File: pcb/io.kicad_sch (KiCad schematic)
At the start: 25 parts

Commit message: Further schematic capture
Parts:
- removed C? (x4): 100n, symbol Device:C
- removed J? (x2): PLR237, adatv2:PLx237, symbol adatv2:PLR237
- removed J? (x2): PLT237, adatv2:PLx237, symbol adatv2:PLT237
- removed L? (x2): 47u, symbol Device:L
- added D?: PRTR5V0U2X, Package_TO_SOT_SMD:SOT-143, symbol Power_Protection:PRTR5V0U2X
- added J?: WORD_CLK_4, symbol Connector:Conn_Coaxial
- added J?: WORD_CLK_3, symbol Connector:Conn_Coaxial
- added R? (x2): 75, symbol Device:R
- added U? (x4): 74LVC1G17, Package_TO_SOT_SMD:SOT-23-5, symbol 74xGxx:74LVC1G17
- R? (x2): value 1k -> 75
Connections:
- net +5V: now also D?.4 (VCC), U?.5 (VCC), U?.5 (VCC), U?.5 (VCC), U?.5 (VCC)
- net GND: now also D?.1 (GND), J?.2 (Ext), J?.2 (Ext), U?.3 (GND), U?.3 (GND), U?.3 (GND), U?.3 (GND)
- net WORD_CLK_1_75_OHM: no longer D?.3 (I/O2), J?.1 (In), R?.2
- net WORD_CLK_1: no longer names the net of R?.1
- net WORD_CLK_1: now also U?.4
- net WORD_CLK_2: no longer names the net of R?.1
- net WORD_CLK_2: now also U?.4
- new net: R?.1, U?.4 (x2)
- new net WORD_CLK: U?.2, U?.2, U?.2, U?.2
- new net WORD_CLK_2_75_OHM: D?.3 (I/O2), J?.1 (In), R?.2
- new net WORD_CLK_3_75_OHM: D?.2 (I/O1), J?.1 (In), R?.2
- new net WORD_CLK_4_75_OHM: D?.3 (I/O2), J?.1 (In), R?.2
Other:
- note removed: "VIN has Vh>2V, so logic level converter is not needed"
- moved on the sheet: D?, H?, J?, R?

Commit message: Further schematic capture
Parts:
- removed R? (x3): 75, symbol Device:R
- removed U? (x4): 74LVC1G17, Package_TO_SOT_SMD:SOT-23-5, symbol 74xGxx:74LVC1G17
- added R? (x7): 150, symbol Device:R
- added U? (x8): 74LVC2G17, symbol 74xGxx:74LVC2G17
- R?: value 75 -> 150
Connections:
- net WORD_CLK: now also U?.1, U?.1, U?.1, U?.1, U?.3, U?.3, U?.3, U?.3
- net WORD_CLK_1_75_OHM: now also R?.2
- net WORD_CLK_2_75_OHM: now also R?.2, R?.2
- net WORD_CLK_3_75_OHM: now also R?.2, R?.2
- net WORD_CLK_4_75_OHM: now also R?.2, R?.2
- net at R?.1: now also U?.6
- new net: R?.1, U?.4 (x4)
- new net: R?.1, U?.6 (x3)
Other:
- moved on the sheet: D?, J?, R?

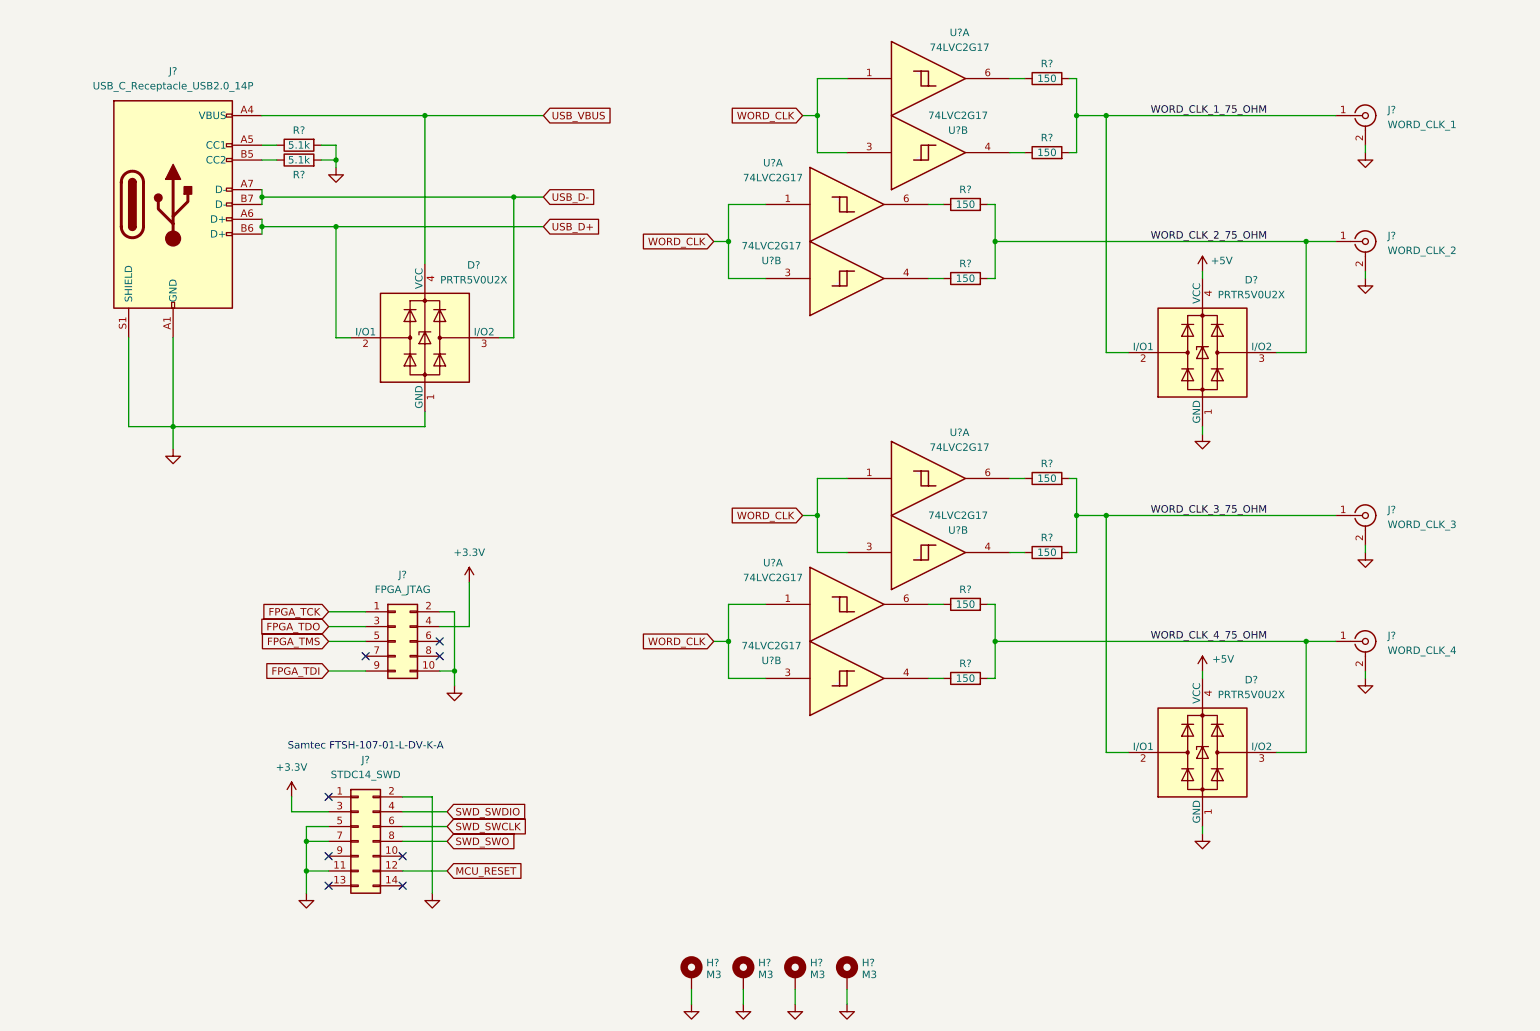
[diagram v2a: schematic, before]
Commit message: Assign most of the footprints to schematic components
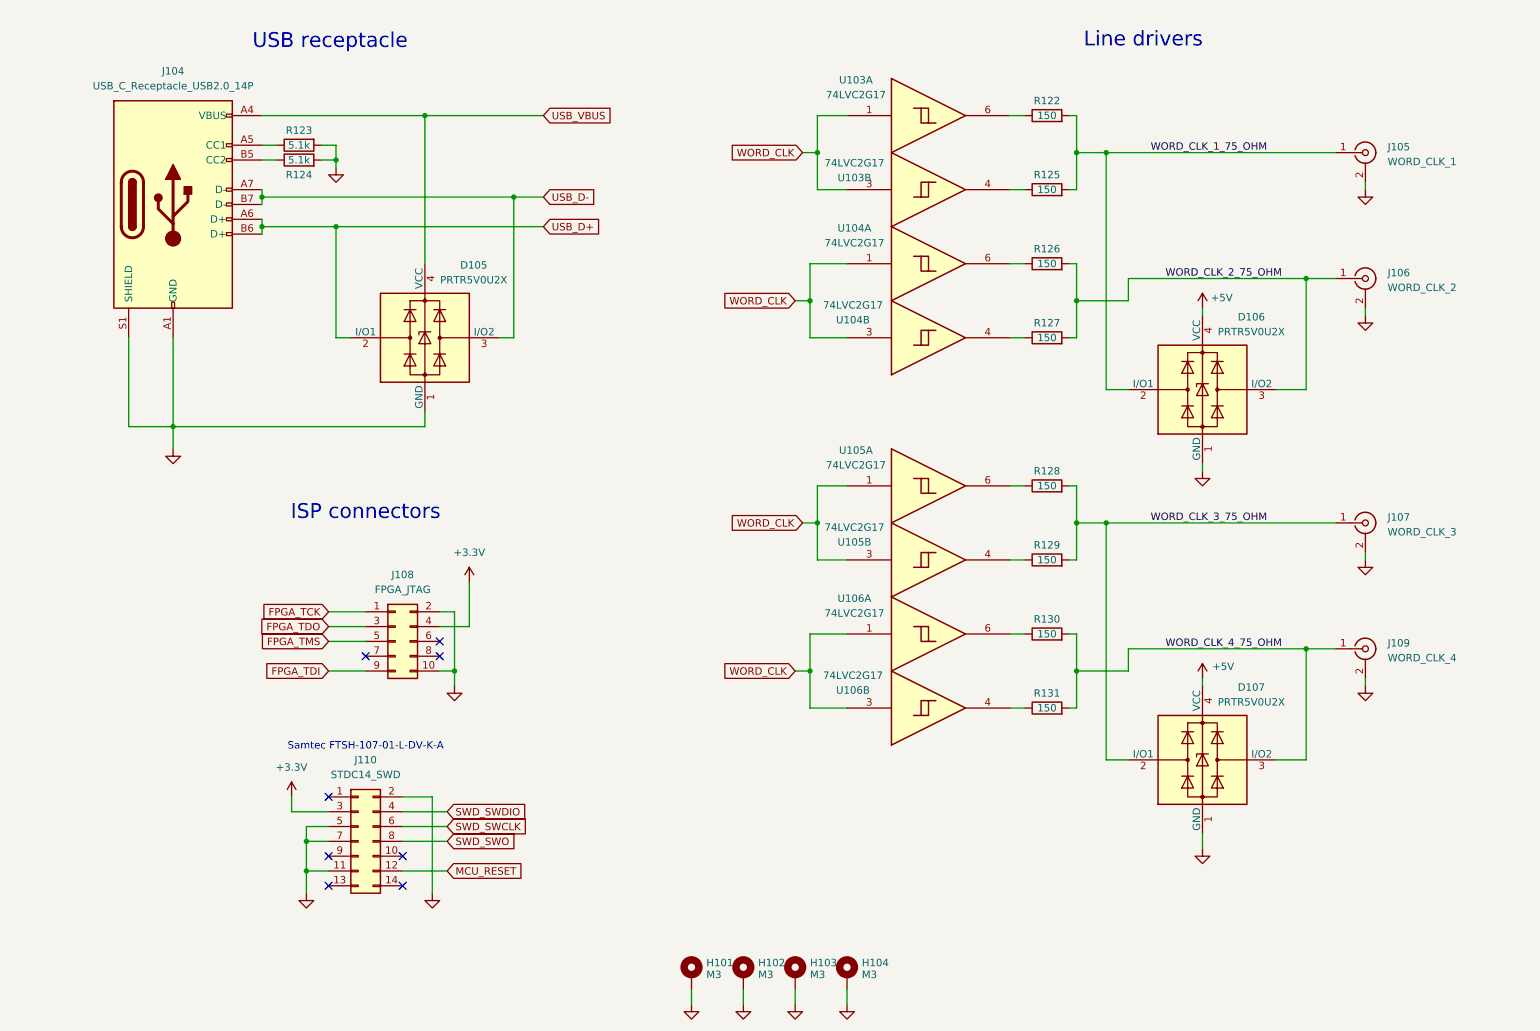
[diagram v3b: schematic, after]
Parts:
- J104: renamed from J?; footprint (none) -> Connector_USB:USB_C_Receptacle_GCT_USB4105-xx-A_16P_TopMnt_Horizontal
- J108: renamed from J?; footprint (none) -> Connector_IDC:IDC-Header_2x05_P2.54mm_Vertical
- R122, R123, R124, R125, R126, R127, R128, R129, R130, R131: renamed from R?; footprint (none) -> Resistor_SMD:R_0805_2012Metric_Pad1.20x1.40mm_HandSolder
- gave numbers to parts that had none: 16
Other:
- note added: "ISP connectors"
- note added: "Line drivers"
- note added: "USB receptacle"
- moved on the sheet: D106, D107, J105, J106, J107, J109, R122, R125, R126, R127, R128, R129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

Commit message: Finish assigning footprints to project
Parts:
- J105, J106, J107: footprint (none) -> adatv2:BNC_dosinconn_DOSIN-801-0051
- J108: renamed from J109; footprint (none) -> Connector_IDC:IDC-Header_2x05_P2.54mm_Vertical
- J109: renamed from J108; footprint Connector_IDC:IDC-Header_2x05_P2.54mm_Vertical -> adatv2:BNC_dosinconn_DOSIN-801-0051
- J110: footprint (none) -> adatv2:Samtec-FTSH-107-01-L-DV-K
- U103, U104, U105, U106: footprint (none) -> Package_TO_SOT_SMD:SOT-23-6_Handsoldering
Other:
- note added: "C10429"
- note added: "C521211"
- note added: "C5563894"
- moved on the sheet: J109
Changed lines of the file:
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@@
 		)
 	)
+	(text "C10429"
+		(exclude_from_sim no)
+		(at 175.006 144.526 0)
+		(effects
+			(font
+				(size 1.27 1.27)
+			)
+		)
+	)
+	(text "C5563894"
+		(exclude_from_sim no)
+		(at 78.74 170.434 0)
+		(effects
+			(font
+				(size 1.27 1.27)
+			)
+		)
+	)
 	(text "Samtec FTSH-107-01-L-DV-K-A"
 		(exclude_from_sim no)
@@
 		)
 	)
+	(text "C521211"
+		(exclude_from_sim no)
+		(at 258.318 44.958 0)
+		(effects
+			(font
+				(size 1.27 1.27)
+			)
+		)
+	)
 	(junction
 		(at 205.74 40.64)
@@
 	)
 	(junction
-		(at 93.98 129.54)
+		(at 87.63 130.81)
 		(diameter 0)
 		(color 0 0 0 0)
@@
 	)
 	(no_connect
-		(at 78.74 127)
+		(at 72.39 128.27)
 	)
 	(no_connect
@@
 	)
 	(no_connect
-		(at 91.44 127)
+		(at 85.09 128.27)
 	)
 	(no_connect
-		(at 91.44 124.46)
+		(at 85.09 125.73)
 	)
 	(no_connect
@@
 	(wire
 		(pts
-			(xy 93.98 129.54) (xy 93.98 132.08)
+			(xy 87.63 130.81) (xy 87.63 133.35)
 		)
 		(stroke
@@
 	(wire
 		(pts
-			(xy 91.44 129.54) (xy 93.98 129.54)
+			(xy 85.09 130.81) (xy 87.63 130.81)
 		)
 		(stroke
@@
 	(wire
 		(pts
-			(xy 93.98 119.38) (xy 93.98 129.54)
+			(xy 87.63 120.65) (xy 87.63 130.81)
 		)
 		(stroke
@@
 	(wire
 		(pts
-			(xy 96.52 114.3) (xy 96.52 121.92)
+			(xy 90.17 115.57) (xy 90.17 123.19)
 		)
 		(stroke
@@
 	(wire
 		(pts
-			(xy 72.39 119.38) (xy 78.74 119.38)
+			(xy 66.04 120.65) (xy 72.39 120.65)
 		)
 		(stroke
@@
 	(wire
 		(pts
-			(xy 72.39 129.54) (xy 78.74 129.54)
+			(xy 66.04 130.81) (xy 72.39 130.81)
 		)
 		(stroke
@@
 	(wire
 		(pts
-			(xy 72.39 124.46) (xy 78.74 124.46)
+			(xy 66.04 125.73) (xy 72.39 125.73)
 		)
 		(stroke
@@
 	(wire
 		(pts
-			(xy 96.52 121.92) (xy 91.44 121.92)
+			(xy 90.17 123.19) (xy 85.09 123.19)
 		)
 		(stroke
@@
 	(wire
 		(pts
-			(xy 91.44 119.38) (xy 93.98 119.38)
+			(xy 85.09 120.65) (xy 87.63 120.65)
 		)
 		(stroke
@@
 	(wire
 		(pts
-			(xy 72.39 121.92) (xy 78.74 121.92)
+			(xy 66.04 123.19) (xy 72.39 123.19)
 		)
 		(stroke
@@
 	(global_label "FPGA_TDO"
 		(shape input)
-		(at 72.39 121.92 180)
+		(at 66.04 123.19 180)
 		(fields_autoplaced yes)
 		(effects
@@
 		)
 		(property "Intersheetrefs" "${INTERSHEET_REFS}"
-			(at 60.1519 121.92 0)
+			(at 53.8019 123.19 0)
 			(effects
 				(font
@@
 	(global_label "FPGA_TMS"
 		(shape input)
-		(at 72.39 124.46 180)
+		(at 66.04 125.73 180)
 		(fields_autoplaced yes)
 		(effects
@@
 		)
 		(property "Intersheetrefs" "${INTERSHEET_REFS}"
-			(at 60.0915 124.46 0)
+			(at 53.7415 125.73 0)
 			(effects
 				(font
@@
 	(global_label "FPGA_TCK"
 		(shape input)
-		(at 72.39 119.38 180)
+		(at 66.04 120.65 180)
 		(fields_autoplaced yes)
 		(effects
@@
 		)
 		(property "Intersheetrefs" "${INTERSHEET_REFS}"
-			(at 60.2124 119.38 0)
+			(at 53.8624 120.65 0)
 			(effects
 				(font
@@
 	(global_label "FPGA_TDI"
 		(shape input)
-		(at 72.39 129.54 180)
+		(at 66.04 130.81 180)
 		(fields_autoplaced yes)
 		(effects
@@
 		)
 		(property "Intersheetrefs" "${INTERSHEET_REFS}"
-			(at 60.8776 129.54 0)
+			(at 54.5276 130.81 0)
 			(effects
 				(font
@@
 			)
 		)
-		(property "Footprint" ""
+		(property "Footprint" "Package_TO_SOT_SMD:SOT-23-6_Handsoldering"
 			(at 176.53 34.29 0)
 			(effects
@@
 		(dnp no)
 		(fields_autoplaced yes)
-		(property "Reference" "J109"
+		(property "Reference" "J108"
 			(at 254 124.7531 0)
 			(effects
@@
 			)
 		)
-		(property "Footprint" ""
+		(property "Footprint" "Connector_IDC:IDC-Header_2x05_P2.54mm_Vertical"
 			(at 250.19 125.73 0)
 			(effects
@@
 			(project "adatv2"
 				(path "/81929cdc-f9fd-4c47-8b7e-bc8597104756/48ac3253-1f5d-4e9f-aed5-ac922c87d2ee"
-					(reference "J109")
+					(reference "J108")
 					(unit 1)
 				)
@@
 	(symbol
 		(lib_id "power:+3.3V")
-		(at 96.52 114.3 0)
+		(at 90.17 115.57 0)
 		(unit 1)
 		(exclude_from_sim no)
@@
 		(fields_autoplaced yes)
 		(property "Reference" "#PWR017"
-			(at 96.52 118.11 0)
+			(at 90.17 119.38 0)
 			(effects
 				(font
@@
 		)
 		(property "Value" "+3.3V"
-			(at 96.52 109.22 0)
+			(at 90.17 110.49 0)
 			(effects
 				(font
@@
 		)
 		(property "Footprint" ""
-			(at 96.52 114.3 0)
+			(at 90.17 115.57 0)
 			(effects
 				(font
@@
 		)
 		(property "Datasheet" ""
-			(at 96.52 114.3 0)
+			(at 90.17 115.57 0)
 			(effects
 				(font
@@
 		)
 		(property "Description" "Power symbol creates a global label with name \"+3.3V\""
-			(at 96.52 114.3 0)
+			(at 90.17 115.57 0)
 			(effects
 				(font
@@
 			)
 		)
-		(property "Footprint" ""
+		(property "Footprint" "Package_TO_SOT_SMD:SOT-23-6_Handsoldering"
 			(at 176.53 46.99 0)
 			(effects
@@
 			)
 		)
-		(property "Footprint" ""
+		(property "Footprint" "adatv2:Samtec-FTSH-107-01-L-DV-K"
 			(at 77.47 158.75 0)
 			(effects
@@
 			)
 		)
-		(property "Footprint" ""
+		(property "Footprint" "Package_TO_SOT_SMD:SOT-23-6_Handsoldering"
 			(at 176.53 110.49 0)
 			(effects
@@
 			)
 		)
-		(property "Footprint" ""
+		(property "Footprint" "Package_TO_SOT_SMD:SOT-23-6_Handsoldering"
 			(at 176.53 123.19 0)
 			(effects
@@
 			)
 		)
-		(property "Footprint" ""
+		(property "Footprint" "Package_TO_SOT_SMD:SOT-23-6_Handsoldering"
 			(at 176.53 97.79 0)
 			(effects
@@
 			)
 		)
-		(property "Footprint" ""
+		(property "Footprint" "adatv2:BNC_dosinconn_DOSIN-801-0051"
 			(at 250.19 62.23 0)
 			(effects
@@
 	(symbol
 		(lib_id "Connector_Generic:Conn_02x05_Odd_Even")
-		(at 83.82 124.46 0)
+		(at 77.47 125.73 0)
 		(unit 1)
 		(exclude_from_sim no)
@@
 		(dnp no)
 		(fields_autoplaced yes)
-		(property "Reference" "J108"
-			(at 85.09 113.03 0)
+		(property "Reference" "J109"
+			(at 78.74 114.3 0)
 			(effects
 				(font
@@
 		)
 		(property "Value" "FPGA_JTAG"
-			(at 85.09 115.57 0)
+			(at 78.74 116.84 0)
 			(effects
 				(font
@@
 			)
 		)
-		(property "Footprint" "Connector_IDC:IDC-Header_2x05_P2.54mm_Vertical"
-			(at 83.82 124.46 0)
+		(property "Footprint" "adatv2:BNC_dosinconn_DOSIN-801-0051"
+			(at 77.47 125.73 0)
 			(effects
 				(font
@@
 		)
 		(property "Datasheet" "~"
-			(at 83.82 124.46 0)
+			(at 77.47 125.73 0)
 			(effects
 				(font
@@
 		)
 		(property "Description" "Generic connector, double row, 02x05, odd/even pin numbering scheme (row 1 odd numbers, row 2 even numbers), script generated (kicad-library-utils/schlib/autogen/connector/)"
-			(at 83.82 124.46 0)
+			(at 77.47 125.73 0)
 			(effects
 				(font
@@
 			(project ""
 				(path "/81929cdc-f9fd-4c47-8b7e-bc8597104756/48ac3253-1f5d-4e9f-aed5-ac922c87d2ee"
-					(reference "J108")
+					(reference "J109")
 					(unit 1)
 				)
@@
 	(symbol
 		(lib_id "power:GND")
-		(at 93.98 132.08 0)
+		(at 87.63 133.35 0)
 		(unit 1)
 		(exclude_from_sim no)
@@
 		(fields_autoplaced yes)
 		(property "Reference" "#PWR018"
-			(at 93.98 138.43 0)
+			(at 87.63 139.7 0)
 			(effects
 				(font
@@
 		)
 		(property "Value" "GND"
-			(at 93.98 137.16 0)
+			(at 87.63 138.43 0)
 			(effects
 				(font
@@
 		)
 		(property "Footprint" ""
-			(at 93.98 132.08 0)
+			(at 87.63 133.35 0)
 			(effects
 				(font
@@
 		)
 		(property "Datasheet" ""
-			(at 93.98 132.08 0)
+			(at 87.63 133.35 0)
 			(effects
 				(font
@@
 		)
 		(property "Description" "Power symbol creates a global label with name \"GND\" , ground"
-			(at 93.98 132.08 0)
+			(at 87.63 133.35 0)
 			(effects
 				(font
@@
 			)
 		)
-		(property "Footprint" ""
+		(property "Footprint" "Package_TO_SOT_SMD:SOT-23-6_Handsoldering"
 			(at 176.53 135.89 0)
 			(effects
@@
 			)
 		)
-		(property "Footprint" ""
+		(property "Footprint" "Package_TO_SOT_SMD:SOT-23-6_Handsoldering"
 			(at 176.53 72.39 0)
 			(effects
@@
 			)
 		)
-		(property "Footprint" ""
+		(property "Footprint" "Package_TO_SOT_SMD:SOT-23-6_Handsoldering"
 			(at 176.53 59.69 0)
 			(effects
@@
 			)
 		)
-		(property "Footprint" ""
+		(property "Footprint" "adatv2:BNC_dosinconn_DOSIN-801-0051"
 			(at 250.19 40.64 0)
 			(effects
@@
 			)
 		)
-		(property "Footprint" ""
+		(property "Footprint" "adatv2:BNC_dosinconn_DOSIN-801-0051"
 			(at 250.19 104.14 0)
 			(effects
